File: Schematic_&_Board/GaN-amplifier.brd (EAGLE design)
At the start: 23 parts, among them T1 FDC3535, T2 NPN_MMBTA06FSCT, U1 TPS7A30XX, X1 SMA-142-0701-801/806, X2 SMA-142-0701-801/806

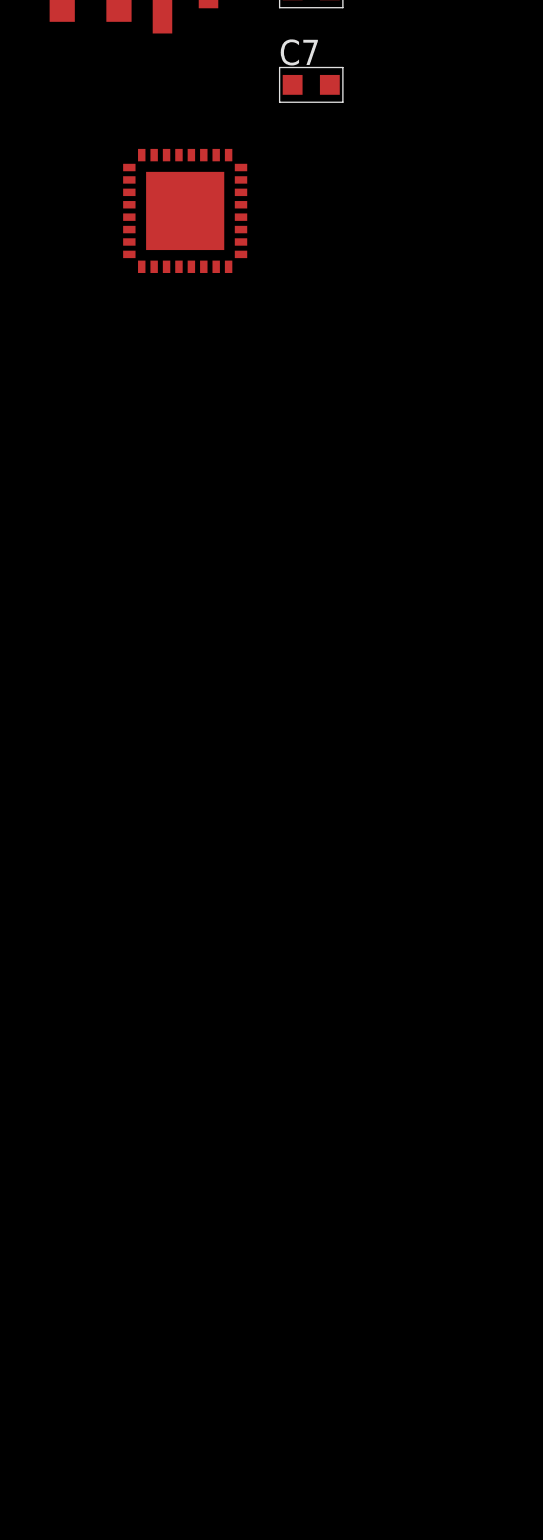
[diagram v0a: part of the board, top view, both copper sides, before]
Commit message: Mostly designed power sequencing
This will all almost certainly be trashed, but it's a start.

DSB
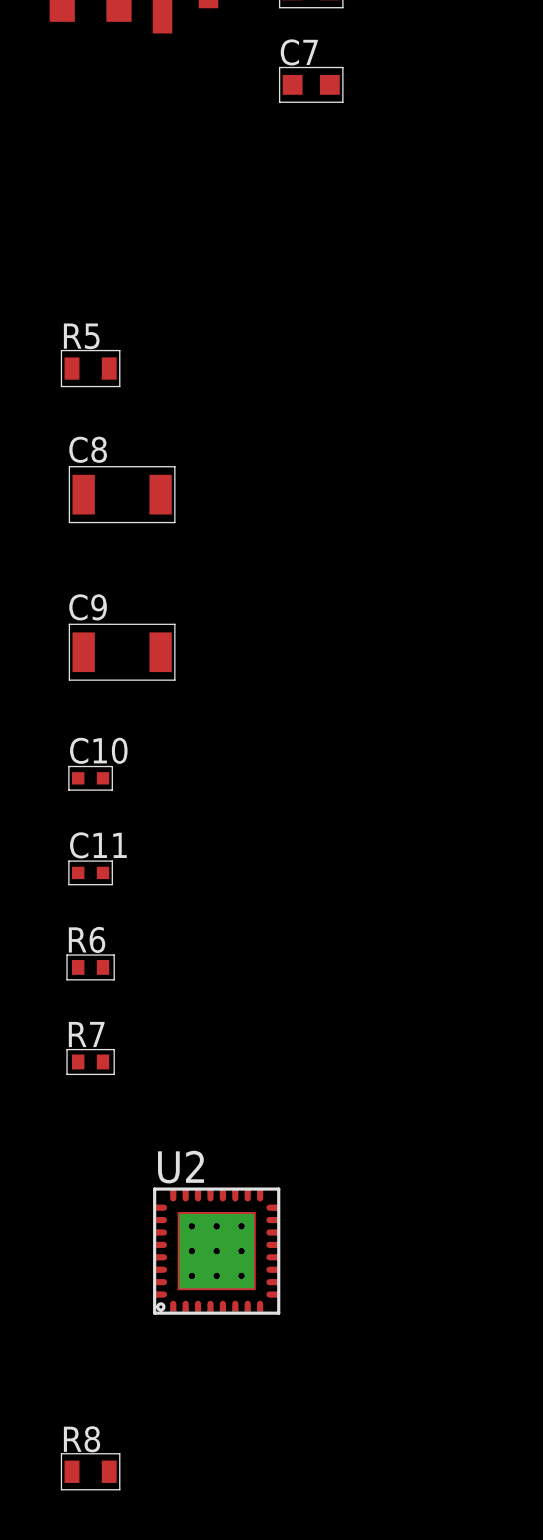
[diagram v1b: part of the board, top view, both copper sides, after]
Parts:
- added C10, C11: 10n, jqi_passives:C_MLCC_0402
- added C8, C9: 10u, jqi_passives:C_MLCC_1206
- added R5: 10k, jqi_passives:R_0603
- added R6, R7: (no value), jqi_passives:R_0402
- added R8: 68.1, jqi_passives:R_0603
- R1: value (none) -> 1k
- R2, R3: value (none) -> 20k
- R4: value (none) -> 90k
- moved U2 41.9 mm to (-68.6, -134.6)
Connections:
- new net -24V: C9.P$1, U1.IN
- new net -8V: C11.P$1, C8.P$1, D1.P$6, R6.P$2, U1.OUT
- new net N$15: C11.P$2, R6.P$1, R7.P$2, U1.FB
- new net N$17: C10.P$1, U1.NR/SS
- net GND: now also C10.P$2, C8.P$2, C9.P$2, R5.P$1, R7.P$1, U1.GND, U1.GND1, U2.12, U2.13, U2.28, U2.29, U2.34, U2.35, U2.36, U2.37, U2.38, U2.39, U2.40, U2.41, U2.42; no longer U2.20, U2.21, U2.4, U2.5
- net N$3: now also R5.P$2

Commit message: Change power sequencing
Switched to using LTC2924 for power sequencing.

DSB
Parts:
- removed D1, D2, D3: BAS16TW, qkdlab_alessandro:SOT-363
- removed D4: 12V, qkdlab_alessandro:SOD123
- removed L2: 0.9u, coilcraft-jqi:1008
- removed R4: 90k, jqi_passives:R_0603
- removed R5: 10k, jqi_passives:R_0603
- added C12: 10u, jqi_passives:C_MLCC_0805
- added C13: 100n, jqi_passives:C_MLCC_0603
- added C14: 0.1u, jqi_passives:C_MLCC_0603
- added IC1: LT3080, regulator-jqi:TO263-5
- added JP1: (no value), pinhead:1X02
- added U3, U5: LT1783, linear-technology-jqi:TSOT-23_S5
- added U4: CPC1117NTR, transistor-jqi:4-LEAD_SOP
- added U6: LTC2924, linear-technology-jqi:SSOP-16_GN
- C1: device jqi_passives:C_MLCC_1210 -> jqi_passives:C_MLCC_0805
- L1: value 5.4n -> 5.4 nH
- R1: value 1k -> 499k
- R2, R3: value 20k -> 10k
- R6: value (none) -> 56k
- R7: value (none) -> 10k
- T1: value FDC3535 -> (none); device qkdlab_alessandro:SUPERSOT-6 -> transistor-jqi:D2PACK
- T2: value NPN_MMBTA06FSCT -> (none); device qkdlab_alessandro:SOT-23 -> transistor-jqi:D2PACK
- U2: value (none) -> HMC1099
- moved R3 253.2 mm to (-85.1, -276.9)
- moved R2 253.2 mm to (-85.1, -273.1)
- moved R1 226.1 mm to (-85.1, -241.3)
- moved C1 205.8 mm to (-83.8, -236.2)
- moved T2 187.0 mm to (-67.3, -199.4)
- moved T1 171.3 mm to (-67.3, -174.0)
- moved L1 57.0 mm to (-81.3, -139.7)
- moved U2 18.2 mm to (-76.2, -151.1)
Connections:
- removed net N$10: D2.P$1, D2.P$5
- removed net N$11: D1.P$3, D2.P$6
- removed net N$12: D1.P$2, D1.P$4
- removed net N$13: D1.P$1, D1.P$5
- removed net N$2: R2.P$1, T2.1
- removed net N$3: R1.P$2, R4.P$1, R5.P$2, T2.2
- removed net N$6: D3.P$2, D3.P$4
- removed net N$7: D3.P$1, D3.P$5
- removed net N$8: D2.P$3, D3.P$6
- removed net N$9: D2.P$2, D2.P$4
- new net +5V: C12.P$1, IC1.3, IC1.6, JP1.1
- new net V+: U3.5, U5.5
- new net V-: U3.2, U5.2
- new net VCC: U6.11
- new net VG_EN: U1.EN
- net +24V: now also IC1.4, IC1.5; no longer D4.C, R3.P$2, R4.P$2, T1.P$4
- net -8V: no longer D1.P$6
- net GND: now also C12.P$2, C13.P$2, R1.P$1, U6.13; no longer R5.P$1, T2.3
- net N$1: now also C13.P$1, IC1.2, R1.P$2; no longer D4.A, R2.P$2, R3.P$1, T1.P$3
- net N$14: no longer T1.P$6
- net N$4: now also JP1.2, U6.16; no longer D3.P$3, R1.P$1

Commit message: Halfway done with power sequencing
The gate voltage supply and bias supply sequencing should be good to
go. Still need to set up the gate voltage and RF power lockout.

DSB
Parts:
- added C15: 150n, jqi_passives:C_MLCC_0603
- added C16: 200n, jqi_passives:C_MLCC_0603
- added C17, C18: 0.1u, jqi_passives:C_MLCC_0603
- added Q1: MMBT3906LT1SMD, transistor-pnp:SOT23-BEC
- added R10: 10k, jqi_passives:R_0603
- added R11: 866, jqi_passives:R_0603
- added R12: 4.42k, jqi_passives:R_0603
- added R13: 1k, jqi_passives:R_0603
- added R14: 2M, jqi_passives:R_0603
- added R15: 54.9k, jqi_passives:R_0603
- added R4: 49.9k, jqi_passives:R_0603
- added R5: 1M, jqi_passives:R_0603
- added R9: 100k, jqi_passives:R_0603
- added T3: IRL3714S, transistor-jqi:D2PACK
- added U7: LCA701S, transistor-jqi:6-LEAD_SMT
- T1, T2: value (none) -> IRL3714S
- moved U4 145.0 mm to (-92.7, -304.8)
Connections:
- removed net N$14: C2.P$1, C3.P$1, C6.P$1
- removed net VCC: U6.11
- removed net VG_EN: U1.EN
- new net AMP_POW: C11.P$1, C18.P$2, C8.P$1, R5.P$2, R6.P$2, T2.3, U1.OUT, U3.2
- new net N$10: Q1.B, R9.P$2
- new net N$11: R13.P$2, T1.3
- new net N$12: R10.P$1, R11.P$1, U3.4
- new net N$13: R13.P$1, U7.1
- new net N$2: R2.P$2, U6.10
- new net N$3: R3.P$2, U6.9
- new net N$5: C16.P$1, U6.14
- new net N$6: R4.P$2, U6.15
- new net N$7: C15.P$1, U6.12
- new net N$8: R11.P$2, R12.P$1, U3.1
- new net N$9: Q1.C, R5.P$1, T2.1
- new net RF_DET: U6.4
- new net RF_EN: U6.8
- new net VDD: C2.P$1, C3.P$1, C6.P$1, R14.P$1, U7.4
- new net VDD_DET: R14.P$2, R15.P$2, U6.2
- new net VDD_EN: T1.1, U6.6
- new net VGG_DET: U6.3
- new net VGG_EN: U6.7
- new net VPIN_DET: R12.P$2, U6.1
- new net VPIN_EN: Q1.E, U6.5
- net +24V: now also U7.6
- net +5V: now also C14.P$1, C17.P$1, R2.P$1, R3.P$1, T1.2, U3.5, U6.11
- net -24V: now also U1.EN
- net -8V: now also R10.P$2, T2.2; no longer C11.P$1, C8.P$1, R6.P$2, U1.OUT
- net GND: now also C14.P$2, C15.P$2, C16.P$2, C17.P$2, C18.P$1, R15.P$1, R4.P$1, R9.P$1, U3.3, U7.2
- net V+: no longer U3.5
- net V-: no longer U3.2

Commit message: Quick Sync to talk sequencing with AR
A few more updates to discuss.

DSB
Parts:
- added R16: 1k, jqi_passives:R_0603
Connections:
- new net N$14: R16.P$2, T3.3
- new net N$16: R16.P$1, U4.P$1
- net +5V: now also T3.2
- net -8V: now also U4.P$4
- net GND: now also U4.P$2
- net VGG_EN: now also T3.1
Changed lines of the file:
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@@
 <element name="R14" library="jqi_passives" package="R_0603" value="2M" x="-100.33" y="-375.92"/>
 <element name="R15" library="jqi_passives" package="R_0603" value="54.9k" x="-100.33" y="-379.73"/>
+<element name="R16" library="jqi_passives" package="R_0603" value="1k" x="-100.33" y="-383.54"/>
 </elements>
 <signals>
@@
 <contactref element="U7" pad="2"/>
 <contactref element="R15" pad="P$1"/>
+<contactref element="U4" pad="P$2"/>
 <wire x1="-77.45" y1="-153.38" x2="-77.95" y2="-153.38" width="0" layer="19" extent="1-1"/>
 <wire x1="-76.95" y1="-153.38" x2="-77.45" y2="-153.38" width="0" layer="19" extent="1-1"/>
@@
 <wire x1="-83.07" y1="-303.53" x2="-83.07" y2="-299.72" width="0" layer="19" extent="1-1"/>
 <wire x1="-85.84" y1="-307.34" x2="-83.07" y2="-303.53" width="0" layer="19" extent="1-1"/>
-<wire x1="-93.46" y1="-323.85" x2="-85.84" y2="-307.34" width="0" layer="19" extent="1-1"/>
+<wire x1="-91.44" y1="-306.197" x2="-85.84" y2="-307.34" width="0" layer="19" extent="1-1"/>
+<wire x1="-93.46" y1="-323.85" x2="-91.44" y2="-306.197" width="0" layer="19" extent="1-1"/>
 <wire x1="-90.69" y1="-327.66" x2="-93.46" y2="-323.85" width="0" layer="19" extent="1-1"/>
 <wire x1="-92.19" y1="-331.47" x2="-90.69" y2="-327.66" width="0" layer="19" extent="1-1"/>
@@
 <contactref element="C17" pad="P$1"/>
 <contactref element="T1" pad="2"/>
+<contactref element="T3" pad="2"/>
 <wire x1="-68.58" y1="-220.98" x2="-67.31" y2="-171.45" width="0" layer="19" extent="1-1"/>
 <wire x1="-68.58" y1="-229.3112" x2="-68.58" y2="-220.98" width="0" layer="19" extent="1-1"/>
@@
 <wire x1="-78.74" y1="-289.56" x2="-84.57" y2="-280.67" width="0" layer="19" extent="1-1"/>
 <wire x1="-92.19" y1="-327.66" x2="-78.74" y2="-289.56" width="0" layer="19" extent="1-1"/>
+<wire x1="-74.93" y1="-351.79" x2="-92.19" y2="-327.66" width="0" layer="19" extent="1-1"/>
 </signal>
 <signal name="V-">
@@
 <contactref element="T2" pad="2"/>
 <contactref element="R10" pad="P$2"/>
-<wire x1="-67.31" y1="-196.85" x2="-91.96" y2="-335.28" width="0" layer="19" extent="1-1"/>
+<contactref element="U4" pad="P$4"/>
+<wire x1="-93.98" y1="-303.403" x2="-91.96" y2="-335.28" width="0" layer="19" extent="1-1"/>
+<wire x1="-67.31" y1="-196.85" x2="-93.98" y2="-303.403" width="0" layer="19" extent="1-1"/>
 </signal>
 <signal name="VPIN_DET">
@@
 <signal name="VGG_EN">
 <contactref element="U6" pad="7"/>
+<contactref element="T3" pad="1"/>
+<wire x1="-85.0138" y1="-269.5575" x2="-77.47" y2="-363.22" width="0" layer="19" extent="1-1"/>
 </signal>
 <signal name="VGG_DET">
@@
 <wire x1="-47.27" y1="-76.2" x2="-53.62" y2="-76.2" width="0" layer="19" extent="1-1"/>
 </signal>
+<signal name="N$14">
+<contactref element="T3" pad="3"/>
+<contactref element="R16" pad="P$2"/>
+<wire x1="-72.39" y1="-363.22" x2="-99.58" y2="-383.54" width="0" layer="19" extent="1-1"/>
+</signal>
+<signal name="N$16">
+<contactref element="R16" pad="P$1"/>
+<contactref element="U4" pad="P$1"/>
+<wire x1="-93.98" y1="-306.197" x2="-101.08" y2="-383.54" width="0" layer="19" extent="1-1"/>
+</signal>
 </signals>

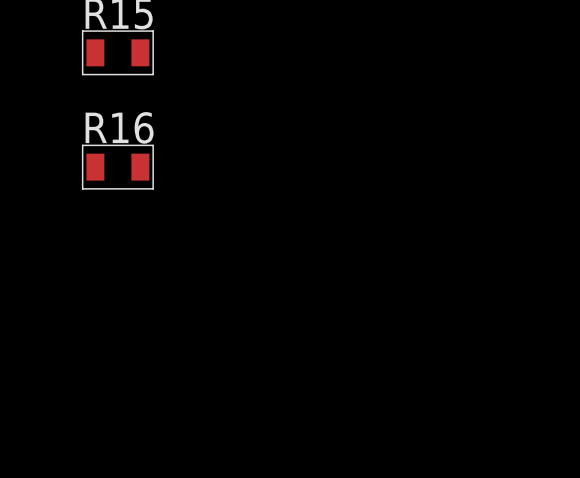
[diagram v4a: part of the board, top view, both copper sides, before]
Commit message: Starting Vgg Control
Started setting up the power sequencing and setpoint control for the
amplifier gate voltage.

DSB
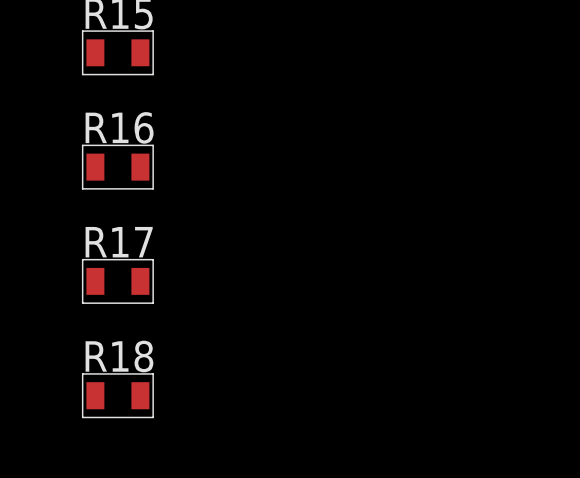
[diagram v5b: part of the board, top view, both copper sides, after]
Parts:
- added R17, R18: 1k, jqi_passives:R_0603
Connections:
- new net VGG: C4.P$1, C5.P$1, C7.P$1, R8.P$1, U4.P$3
- net GND: now also R18.P$2
- net N$14: now also R17.P$1
- net VGG_DET: now also R17.P$2, R18.P$1
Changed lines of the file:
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@@
 <element name="R15" library="jqi_passives" package="R_0603" value="54.9k" x="-100.33" y="-379.73"/>
 <element name="R16" library="jqi_passives" package="R_0603" value="1k" x="-100.33" y="-383.54"/>
+<element name="R17" library="jqi_passives" package="R_0603" value="1k" x="-100.33" y="-387.35"/>
+<element name="R18" library="jqi_passives" package="R_0603" value="1k" x="-100.33" y="-391.16"/>
 </elements>
 <signals>
@@
 <contactref element="R15" pad="P$1"/>
 <contactref element="U4" pad="P$2"/>
+<contactref element="R18" pad="P$2"/>
+<wire x1="-101.08" y1="-379.73" x2="-99.58" y2="-391.16" width="0" layer="19" extent="1-1"/>
+<wire x1="-99.06" y1="-366.4" x2="-101.08" y2="-379.73" width="0" layer="19" extent="1-1"/>
+<wire x1="-92.19" y1="-331.47" x2="-99.06" y2="-366.4" width="0" layer="19" extent="1-1"/>
+<wire x1="-90.69" y1="-327.66" x2="-92.19" y2="-331.47" width="0" layer="19" extent="1-1"/>
+<wire x1="-93.46" y1="-323.85" x2="-90.69" y2="-327.66" width="0" layer="19" extent="1-1"/>
+<wire x1="-91.44" y1="-306.197" x2="-93.46" y2="-323.85" width="0" layer="19" extent="1-1"/>
+<wire x1="-85.84" y1="-307.34" x2="-91.44" y2="-306.197" width="0" layer="19" extent="1-1"/>
+<wire x1="-83.07" y1="-303.53" x2="-85.84" y2="-307.34" width="0" layer="19" extent="1-1"/>
+<wire x1="-83.07" y1="-299.72" x2="-83.07" y2="-303.53" width="0" layer="19" extent="1-1"/>
+<wire x1="-83.07" y1="-280.67" x2="-83.07" y2="-299.72" width="0" layer="19" extent="1-1"/>
+<wire x1="-80.0862" y1="-267.6525" x2="-83.07" y2="-280.67" width="0" layer="19" extent="1-1"/>
+<wire x1="-84.963" y1="-257.49" x2="-80.0862" y2="-267.6525" width="0" layer="19" extent="1-1"/>
+<wire x1="-83.07" y1="-251.46" x2="-84.963" y2="-257.49" width="0" layer="19" extent="1-1"/>
+<wire x1="-82.87" y1="-246.38" x2="-83.07" y2="-251.46" width="0" layer="19" extent="1-1"/>
+<wire x1="-85.84" y1="-241.3" x2="-82.87" y2="-246.38" width="0" layer="19" extent="1-1"/>
+<wire x1="-82.87" y1="-236.22" x2="-85.84" y2="-241.3" width="0" layer="19" extent="1-1"/>
+<wire x1="-77.95" y1="-153.38" x2="-82.87" y2="-236.22" width="0" layer="19" extent="1-1"/>
 <wire x1="-77.45" y1="-153.38" x2="-77.95" y2="-153.38" width="0" layer="19" extent="1-1"/>
 <wire x1="-76.95" y1="-153.38" x2="-77.45" y2="-153.38" width="0" layer="19" extent="1-1"/>
@@
 <wire x1="-38.69" y1="-39.37" x2="-44.17" y2="-76.2" width="0" layer="19" extent="1-1"/>
 <wire x1="-39.665" y1="-37.27" x2="-38.69" y2="-39.37" width="0" layer="19" extent="1-1"/>
-<wire x1="-82.87" y1="-236.22" x2="-77.95" y2="-153.38" width="0" layer="19" extent="1-1"/>
-<wire x1="-85.84" y1="-241.3" x2="-82.87" y2="-236.22" width="0" layer="19" extent="1-1"/>
-<wire x1="-82.87" y1="-246.38" x2="-85.84" y2="-241.3" width="0" layer="19" extent="1-1"/>
-<wire x1="-83.07" y1="-251.46" x2="-82.87" y2="-246.38" width="0" layer="19" extent="1-1"/>
-<wire x1="-84.963" y1="-257.49" x2="-83.07" y2="-251.46" width="0" layer="19" extent="1-1"/>
-<wire x1="-80.0862" y1="-267.6525" x2="-84.963" y2="-257.49" width="0" layer="19" extent="1-1"/>
-<wire x1="-83.07" y1="-280.67" x2="-80.0862" y2="-267.6525" width="0" layer="19" extent="1-1"/>
-<wire x1="-83.07" y1="-299.72" x2="-83.07" y2="-280.67" width="0" layer="19" extent="1-1"/>
-<wire x1="-83.07" y1="-303.53" x2="-83.07" y2="-299.72" width="0" layer="19" extent="1-1"/>
-<wire x1="-85.84" y1="-307.34" x2="-83.07" y2="-303.53" width="0" layer="19" extent="1-1"/>
-<wire x1="-91.44" y1="-306.197" x2="-85.84" y2="-307.34" width="0" layer="19" extent="1-1"/>
-<wire x1="-93.46" y1="-323.85" x2="-91.44" y2="-306.197" width="0" layer="19" extent="1-1"/>
-<wire x1="-90.69" y1="-327.66" x2="-93.46" y2="-323.85" width="0" layer="19" extent="1-1"/>
-<wire x1="-92.19" y1="-331.47" x2="-90.69" y2="-327.66" width="0" layer="19" extent="1-1"/>
-<wire x1="-99.06" y1="-366.4" x2="-92.19" y2="-331.47" width="0" layer="19" extent="1-1"/>
-<wire x1="-101.08" y1="-379.73" x2="-99.06" y2="-366.4" width="0" layer="19" extent="1-1"/>
 </signal>
 <signal name="N$15">
@@
 <signal name="VGG_DET">
 <contactref element="U6" pad="3"/>
+<contactref element="R17" pad="P$2"/>
+<contactref element="R18" pad="P$1"/>
+<wire x1="-99.58" y1="-387.35" x2="-101.08" y2="-391.16" width="0" layer="19" extent="1-1"/>
+<wire x1="-85.0138" y1="-267.0175" x2="-99.58" y2="-387.35" width="0" layer="19" extent="1-1"/>
 </signal>
 <signal name="RF_DET">
@@
 <contactref element="T3" pad="3"/>
 <contactref element="R16" pad="P$2"/>
+<contactref element="R17" pad="P$1"/>
+<wire x1="-99.58" y1="-383.54" x2="-101.08" y2="-387.35" width="0" layer="19" extent="1-1"/>
 <wire x1="-72.39" y1="-363.22" x2="-99.58" y2="-383.54" width="0" layer="19" extent="1-1"/>
 </signal>
@@
 <wire x1="-93.98" y1="-306.197" x2="-101.08" y2="-383.54" width="0" layer="19" extent="1-1"/>
 </signal>
+<signal name="VGG">
+<contactref element="U4" pad="P$3"/>
+<contactref element="C4" pad="P$1"/>
+<contactref element="R8" pad="P$1"/>
+<contactref element="C5" pad="P$1"/>
+<contactref element="C7" pad="P$1"/>
+<wire x1="-65.52" y1="-87.63" x2="-74.41" y2="-143.51" width="0" layer="19" extent="1-1"/>
+<wire x1="-66.32" y1="-76.2" x2="-65.52" y2="-87.63" width="0" layer="19" extent="1-1"/>
+<wire x1="-59.97" y1="-76.2" x2="-66.32" y2="-76.2" width="0" layer="19" extent="1-1"/>
+<wire x1="-91.44" y1="-303.403" x2="-74.41" y2="-143.51" width="0" layer="19" extent="1-1"/>
+</signal>
 </signals>

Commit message: Finished Power Sequencing
Completed the power sequencing section. Starting on the RF amp section.
Need to track down the correct inductors.

DSB
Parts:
- added C19, C20: 10u, jqi_passives:C_MLCC_1210
- added C21, C23, C24: 2.2n, jqi_passives:C_MLCC_0603
- added C22: 0.1u, jqi_passives:C_MLCC_0603
- added C25, C26: 3.3p, jqi_passives:C_MLCC_0603
- added JP2: (no value), pinhead:1X02
- added L2: 5.6n, jqi_passives:R_0402
- added R19, R25, R26: 200, jqi_passives:R_0603
- added R20, R27: 100, jqi_passives:R_0603
- added R21: 500, rlc-jqi:3269P
- added R22: 1k, jqi_passives:R_0603
- added R23: 200k, jqi_passives:R_0603
- added R24: 51k, jqi_passives:R_0603
- added R28: 4k, jqi_passives:R_0603
- added R29: 0.05, rlc-jqi:1206_KELVIN
- added T4: IRL3714S, transistor-jqi:D2PACK
- added T5: BSP89, transistor-jqi:PG-SOT-223
- added X3: BNC-V, connector-jqi:BNC-V
- R17: value 1k -> 200k
- R18: value 1k -> 51k
- U5: value LT1783 -> LT6015
- moved U5 224.0 mm to (-99.1, -485.1)
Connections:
- removed net V+: U5.5
- removed net V-: U5.2
- removed net VGG: C4.P$1, C5.P$1, C7.P$1, R8.P$1, U4.P$3
- new net N$18: C4.P$1, C5.P$1, C7.P$1, R21.2, R8.P$1
- new net N$19: R19.P$2, R21.3
- new net N$20: R20.P$1, R21.1
- new net N$21: R22.P$2, R23.P$1, T4.3
- new net N$22: JP2.1, R22.P$1
- new net N$23: R26.P$1, U5.4
- new net N$24: R25.P$2, T5.2, T5.4, U5.3
- new net N$25: R27.P$2, U5.1
- new net N$26: R27.P$1, T5.1
- new net N$27: R25.P$1, R29.P$2
- new net N$28: R28.P$1, T5.3, X3.1
- new net N$29: R26.P$2, R29.P$1
- new net N$30: C23.P$1, X2.1
- new net N$31: C24.P$2, X1.1
- new net N$33: C23.P$2, C25.P$1, L1.P$2
- new net N$34: L1.P$1, U2.20, U2.21
- new net N$35: C24.P$1, C26.P$1, L2.P$1
- new net V_PINCH: L2.P$2, R8.P$2, U2.4, U2.5, U4.P$3
- net +5V: now also C22.P$2, T4.2, U5.5
- net -8V: now also C19.P$1, C20.P$1, C21.P$1, R19.P$1
- net GND: now also C19.P$2, C20.P$2, C21.P$2, C22.P$1, C25.P$2, C26.P$2, JP2.2, R20.P$2, R24.P$2, R28.P$2, U5.2, X1.G@1, X1.G@2, X1.G@3, X1.G@4, X2.G@1, X2.G@2, X2.G@3, X2.G@4, X3.2
- net RF_DET: now also R23.P$2, R24.P$1
- net RF_EN: now also T4.1
- net VDD: now also R29.P$4

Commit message: Finished Schematic
Found a bias inductor, so the schematic is finished. I'll want to get
the board layed out this week so that a test piece can be ordered before
Xmas.

DSB
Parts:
- added L3: 0.9u, coilcraft-jqi:1008
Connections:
- new net N$32: L3.P$2, R29.P$3
- net N$34: now also L3.P$1
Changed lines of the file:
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@@
 <element name="C26" library="jqi_passives" package="C_MLCC_0603" value="3.3p" x="-100.33" y="-576.58"/>
 <element name="L2" library="jqi_passives" package="R_0402" value="5.6n" x="-100.33" y="-580.39"/>
+<element name="L3" library="coilcraft-jqi" package="1008" value="0.9u" x="-107.95" y="-576.58">
+<attribute name="COILCRAFT" value="1008AF" x="-107.95" y="-576.58" size="1.778" layer="27" display="off"/>
+</element>
 </elements>
 <signals>
@@
 <contactref element="U2" pad="20"/>
 <contactref element="L1" pad="P$1"/>
+<contactref element="L3" pad="P$1"/>
 <wire x1="-75.95" y1="-148.88" x2="-76.45" y2="-148.88" width="0" layer="19" extent="1-1"/>
 <wire x1="-82.1944" y1="-140.208" x2="-76.45" y2="-148.88" width="0" layer="19" extent="1-1"/>
+<wire x1="-109.093" y1="-576.58" x2="-76.45" y2="-148.88" width="0" layer="19" extent="1-1"/>
 </signal>
 <signal name="N$35">
@@
 <wire x1="-97.917" y1="-486.09" x2="-101.08" y2="-506.73" width="0" layer="19" extent="1-1"/>
 </signal>
+<signal name="N$32">
+<contactref element="R29" pad="P$3"/>
+<contactref element="L3" pad="P$2"/>
+<wire x1="-99.06" y1="-560.2" x2="-106.807" y2="-576.58" width="0" layer="19" extent="1-1"/>
+</signal>
 </signals>
